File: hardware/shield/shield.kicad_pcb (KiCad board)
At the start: 2 copper layers, 83 parts, among them J1 Conn_01x18, J10 Conn_01x09, J11 Conn_01x03, J12 Conn_01x03, J13 Conn_01x04, J14 DCDC, J15 Conn_01x01_Pin, J16 Conn_01x01_Pin, J17 Conn_01x01_Pin, J18 Conn_01x01_Pin, J19 Conn_01x01_Pin, J2 Conn_01x20, J20 Conn_01x01_Pin, J21 Conn_01x01_Pin, J22 Conn_01x01_Pin, J23 Conn_01x01_Pin, J24 Conn_01x03, J25 Conn_01x03, J26 Conn_01x04, J27 Conn_01x03, J28 Conn_01x03, J29 Conn_01x03, J3 Conn_01x20, J30 Conn_01x03, J31 Conn_01x03, J32 Conn_01x08, J33 Conn_01x04, J34 DCDC, J35 Conn_01x03, J4 BAT, J5 DCDC, J6 DCDC, J7 Conn_01x03, J8 Conn_01x03, J9 Conn_01x10, U1 NUCLEO-N657X0-Q, U2 AMS1117-3.3

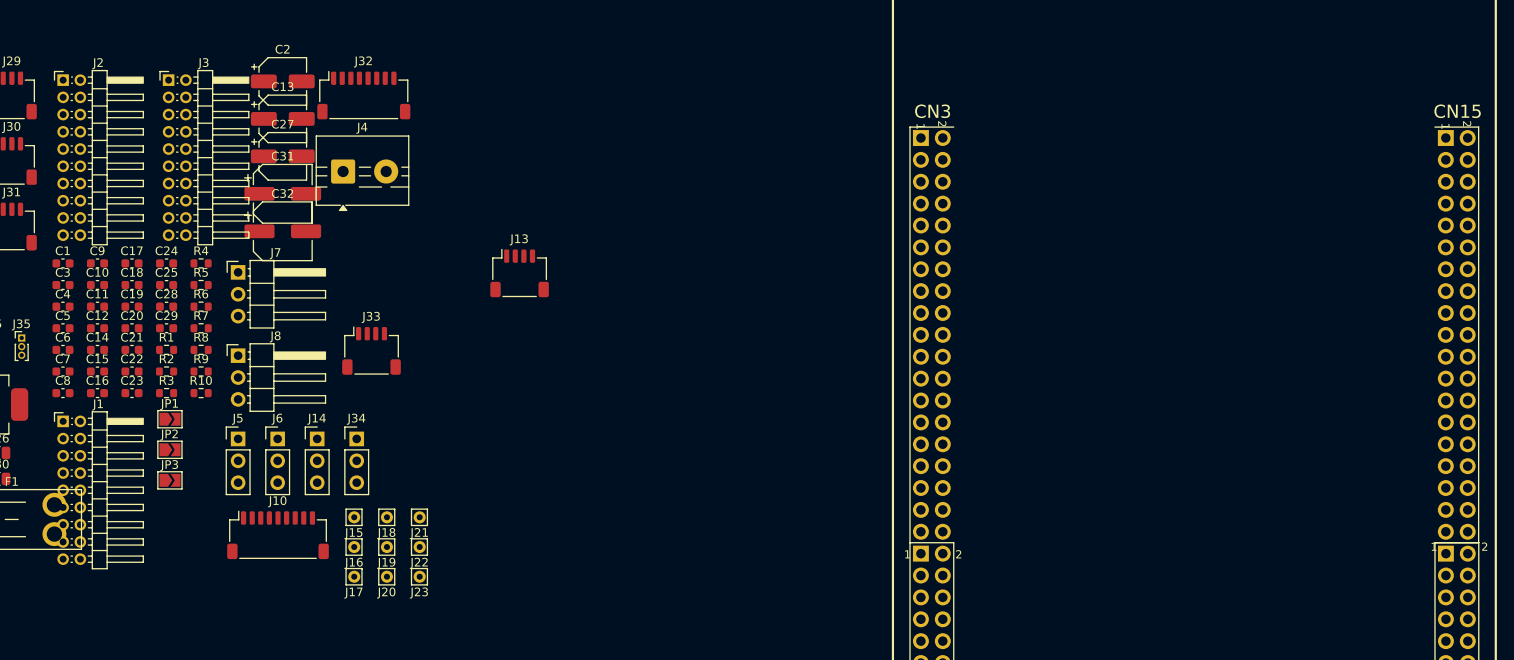
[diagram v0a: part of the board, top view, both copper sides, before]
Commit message: larger pin headers
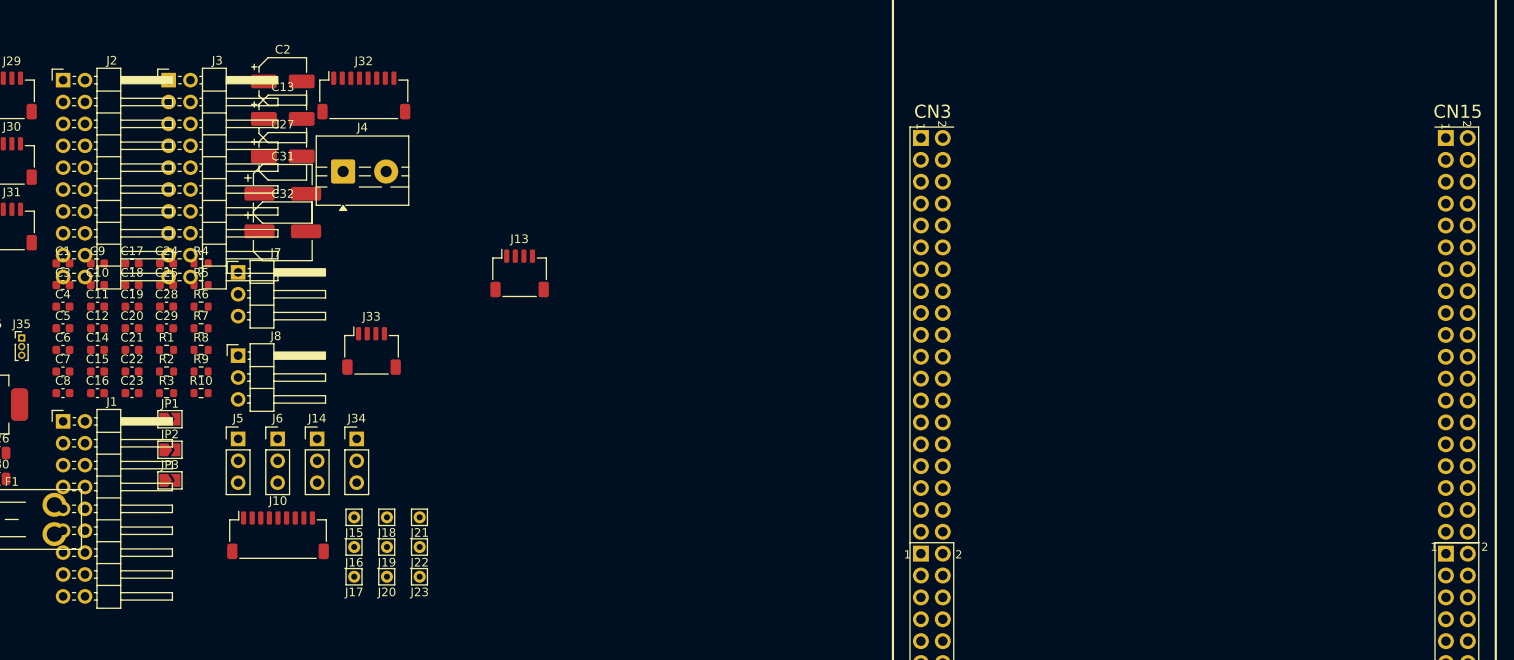
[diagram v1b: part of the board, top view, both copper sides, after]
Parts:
- J1: footprint Connector_PinHeader_2.00mm:PinHeader_2x09_P2.00mm_Horizontal -> Connector_PinHeader_2.54mm:PinHeader_2x09_P2.54mm_Horizontal
- J2, J3: footprint Connector_PinHeader_2.00mm:PinHeader_2x10_P2.00mm_Horizontal -> Connector_PinHeader_2.54mm:PinHeader_2x10_P2.54mm_Horizontal

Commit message: Approx layout done
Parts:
- J1: value Conn_01x18 -> CAMERA
- J10: value Conn_01x09 -> UI_MODULE
- J11: value Conn_01x03 -> RX_PWM
- J12: value Conn_01x03 -> CMD_RX
- J13: value Conn_01x04 -> TEL_UART
- J14: value DCDC -> 5V_DCDC_2
- J15: value Conn_01x01_Pin -> 5V_TP1
- J16: value Conn_01x01_Pin -> 5V_TP2
- J17: value Conn_01x01_Pin -> 3V3_TP3
- J18: value Conn_01x01_Pin -> 3V3_TP4
- J19: value Conn_01x01_Pin -> GND_TP1
- J2: value Conn_01x20 -> LINE_FRONT
- J20: value Conn_01x01_Pin -> GND_TP2
- J21: value Conn_01x01_Pin -> GND_TP3
- J22: value Conn_01x01_Pin -> GND_TP4
- J23: value Conn_01x01_Pin -> GND
- J24: value Conn_01x03 -> UART
- J25: value Conn_01x03 -> SPI
- J26: value Conn_01x04 -> PINS
- J27: value Conn_01x03 -> LED_DATA
- J28: value Conn_01x03 -> IR_1
- J29: value Conn_01x03 -> IR_2
- J3: value Conn_01x20 -> LINE_BACK
- J30: value Conn_01x03 -> IR_3
- J31: value Conn_01x03 -> IR_4
- J32: value Conn_01x08 -> MOTOR_DRIVER
- J33: value Conn_01x04 -> ENC_AB
- J34: value DCDC -> 8V_DCDC_2
- J35: value Conn_01x03 -> I2C4
- J5: value DCDC -> 5V_DCDC_1
- J6: value DCDC -> 8V_DCDC_1
- J7: value Conn_01x03 -> SERVO_BACK
- J8: value Conn_01x03 -> SERVO_FRONT
- J9: value Conn_01x10 -> IMU
- JP1: value SolderJumper_2_Open -> 5V_1
- JP2: value SolderJumper_2_Open -> 5V_2
- JP3: value SolderJumper_2_Open -> 3V3
- moved J1 175.6 mm to (232.5, 45.0)
- moved J2 174.2 mm to (232.5, 78.6)
- moved C6 169.9 mm to (221.5, 133.6), turned to 90 degrees
- moved J8 162.6 mm to (235.0, 131.7)
- moved U1 159.3 mm to (35.4, 51.8), turned to -90 degrees
- moved R2 157.4 mm to (228.0, 49.5), turned to 90 degrees
- moved C32 155.9 mm to (227.5, 130.3), turned to 90 degrees
- moved R1 155.0 mm to (225.5, 46.8), turned to 90 degrees
- moved F1 146.4 mm to (186.9, 41.4), turned to 180 degrees
- moved J30 136.3 mm to (191.6, 62.2), turned to 90 degrees
- moved J31 136.0 mm to (191.1, 72.7), turned to 90 degrees
- moved J28 131.6 mm to (179.0, 62.3), turned to 90 degrees
- moved J29 126.1 mm to (179.0, 72.8), turned to 90 degrees
- moved C5 123.5 mm to (182.0, 47.3), turned to -90 degrees
- moved C21 121.7 mm to (189.5, 56.9), turned to 90 degrees
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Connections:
- J27 pad 2: Net-(J27-Pin_2) -> 5V_EXT
- J27 pad 3: 5V_EXT -> Net-(J27-Pin_3)
- R5 pad 1: Net-(J27-Pin_2) -> Net-(J27-Pin_3)
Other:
- board outline added: 230 x 110 mm

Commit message: PCB v1 done
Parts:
- moved J25 186.9 mm to (202.0, 87.5), turned to 0 degrees
- moved C14 129.2 mm to (216.2, 111.4)
- moved J13 129.2 mm to (218.7, 116.9)
- moved C4 128.8 mm to (224.5, 137.7)
- moved C1 128.6 mm to (33.0, 35.5), turned to 90 degrees
- moved J34 128.5 mm to (37.0, 35.0)
- moved C13 127.3 mm to (201.5, 131.1), turned to 180 degrees
- moved JP2 126.8 mm to (201.5, 136.9)
- moved C12 126.2 mm to (196.4, 133.7)
- moved J14 123.8 mm to (210.0, 124.9)
- moved J6 122.2 mm to (219.5, 133.2)
- moved C27 120.4 mm to (174.0, 73.0)
- moved JP3 120.4 mm to (192.5, 78.8)
- moved U2 120.4 mm to (184.7, 74.3)
- moved C26 120.4 mm to (192.9, 74.3)
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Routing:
- net 3V3: track 0.00 -> 492.8 mm, vias 0 -> 13
- net VBAT: track 0.00 -> 471.4 mm, vias 0 -> 1
- net 5V: track 0.00 -> 334.4 mm, vias 0 -> 8
- net /LINE_AD_CS2: track 0.00 -> 304.3 mm, vias 0 -> 3
- net /LINE_AD_CS1: track 0.00 -> 301.7 mm, vias 0 -> 8
- net /LINE_LED_OE: track 0.00 -> 273.0 mm, vias 0 -> 4
- net /TEL_TX: track 0.00 -> 253.3 mm, vias 0 -> 6
- net /LINE_SPI4_SCK: track 0.00 -> 251.4 mm, vias 0 -> 2
- net /OV_I2C4_SCL: track 0.00 -> 250.4 mm, vias 0 -> 13
- net /LINE_AD_CS3: track 0.00 -> 248.6 mm, vias 0 -> 7
- net /LINE_INF_OE: track 0.00 -> 240.9 mm, vias 0 -> 7
- net /LINE_INF_LE: track 0.00 -> 238.1 mm, vias 0 -> 7
- net /LINE_LED_LE: track 0.00 -> 235.1 mm, vias 0 -> 7
- net /SERVO_FRONT: track 0.00 -> 234.0 mm, vias 0 -> 11
- net /LINE_SPI4_MOSI: track 0.00 -> 234.0 mm, vias 0 -> 1
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- added copper zone on B.Cu, net GND
- added copper zone on F.Cu, net GND

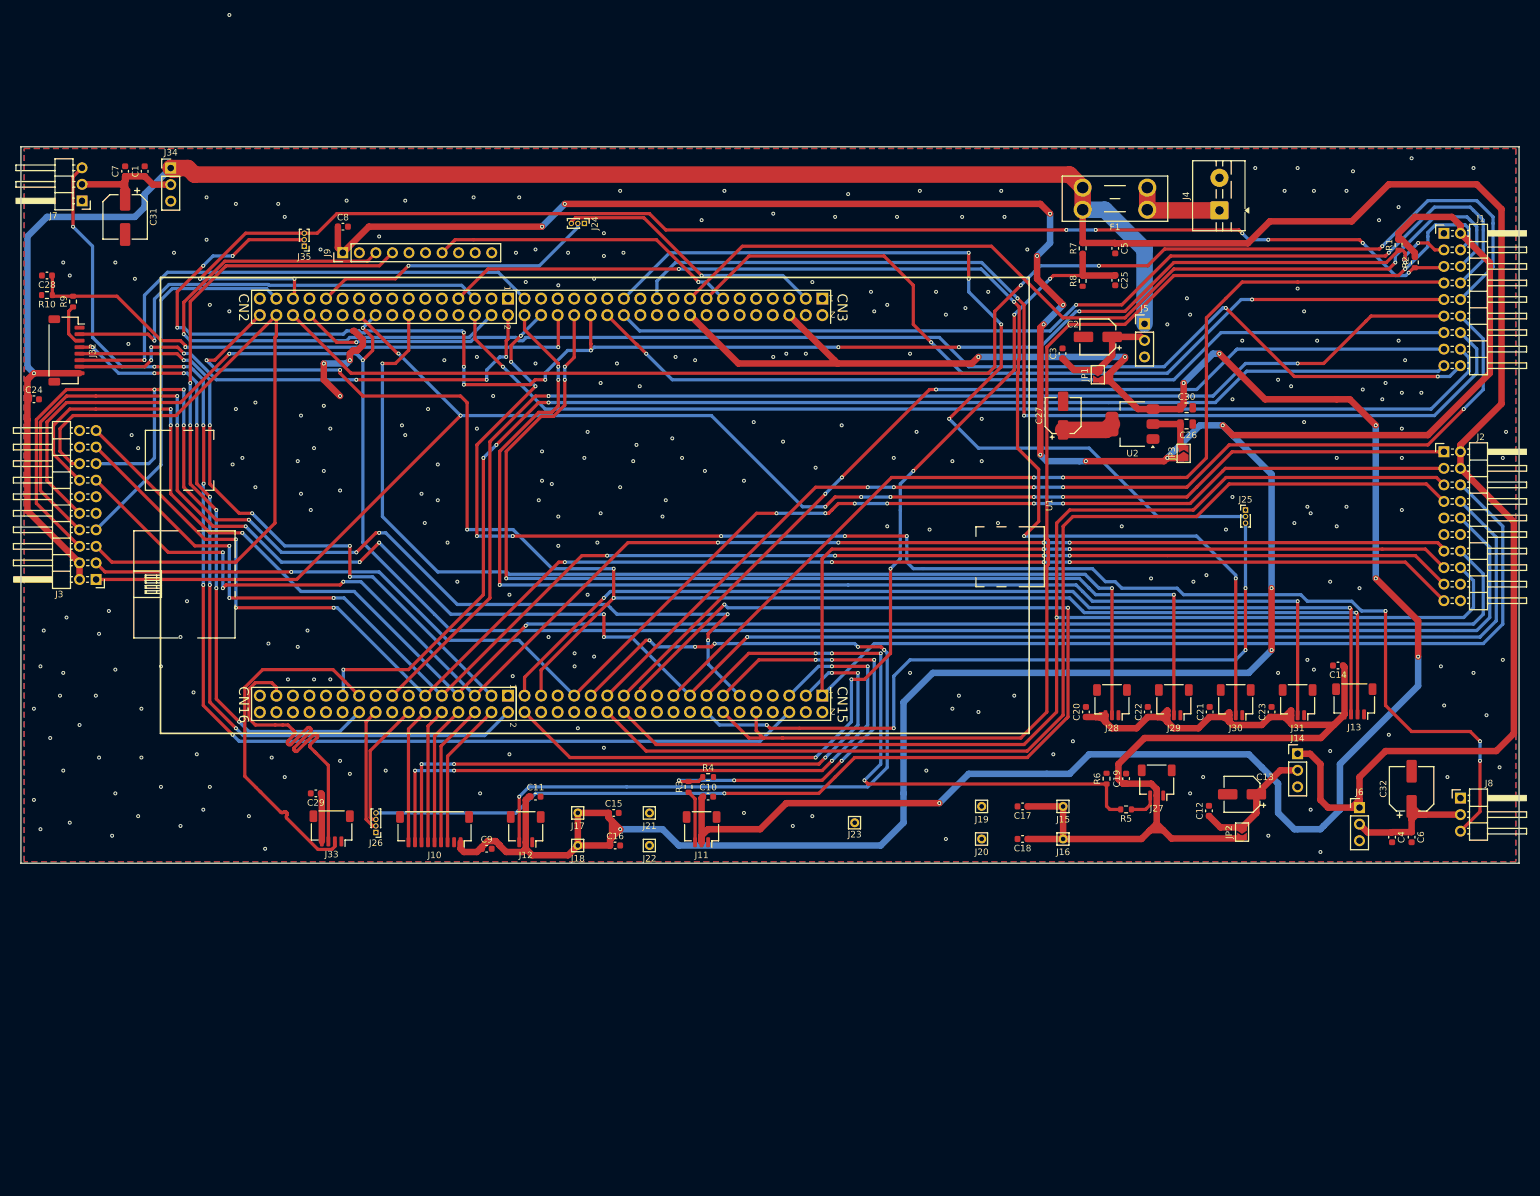
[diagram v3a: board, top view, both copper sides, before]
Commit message: Fixed DRCs, added labels to silkscreen
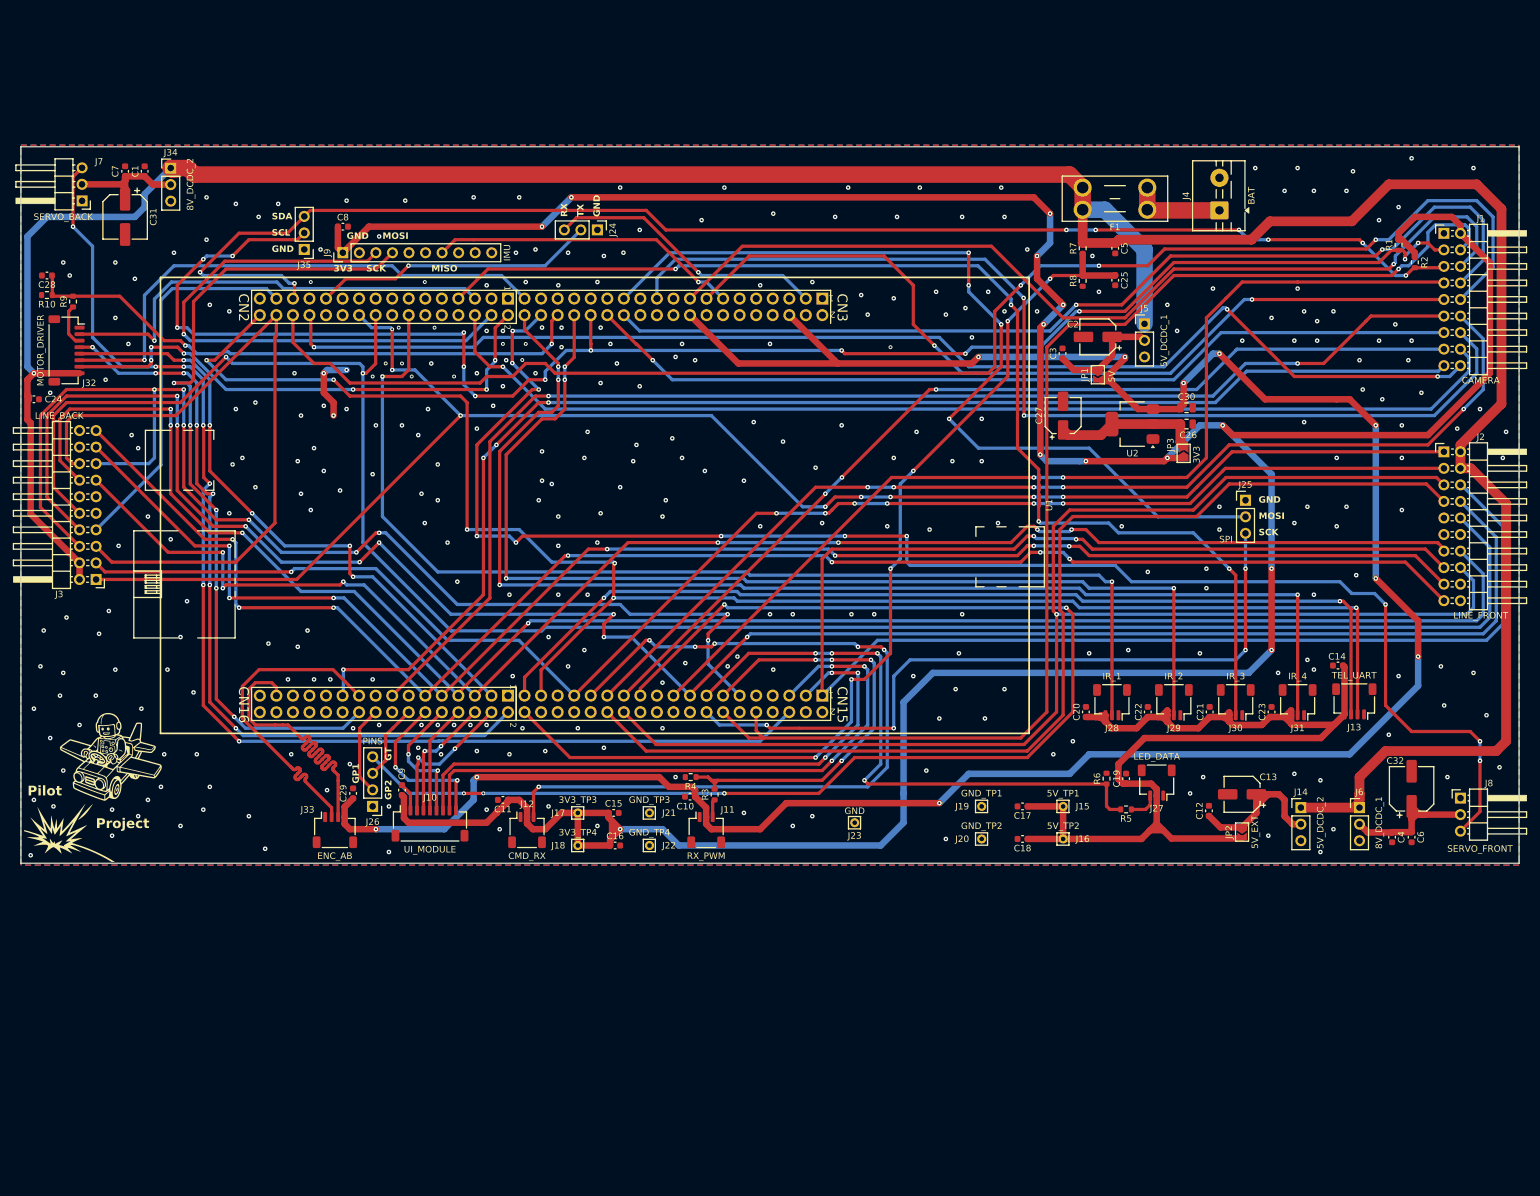
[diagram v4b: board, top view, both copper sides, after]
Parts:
- added G***: LOGO, LOGO, F.Cu at (29.5, 130.0)
- J24, J25, J35: footprint Connector_PinHeader_1.00mm:PinHeader_1x03_P1.00mm_Vertical -> Connector_PinHeader_2.54mm:PinHeader_1x03_P2.54mm_Vertical
- J26: footprint Connector_PinHeader_1.00mm:PinHeader_1x04_P1.00mm_Vertical -> Connector_PinHeader_2.54mm:PinHeader_1x04_P2.54mm_Vertical
- JP1: value 5V_1 -> 5V
- JP2: value 5V_2 -> 5V_EXT
- moved C9 15.8 mm to (72.5, 130.5), turned to 90 degrees
- moved J14 8.28 mm to (210.5, 133.2)
- moved C29 5.73 mm to (65.0, 131.0), turned to 90 degrees
- moved C11 5.02 mm to (88.0, 132.0), turned to 180 degrees
- moved R3 4.17 mm to (120.5, 131.2)
- moved J26 4.03 mm to (68.0, 133.0)
- moved C10 2.78 mm to (116.7, 131.5), turned to 180 degrees
- moved R4 2.67 mm to (116.8, 128.5), turned to 180 degrees
- moved J24 2.24 mm to (102.5, 44.5)
- moved J25 1.50 mm to (202.0, 86.0)
- moved J10 1.12 mm to (76.8, 135.6), turned to 0 degrees
- moved J11 0.71 mm to (119.2, 136.6), turned to 0 degrees
- moved J33 0.56 mm to (62.2, 136.6), turned to 0 degrees
- moved J35 0.50 mm to (57.5, 47.5)
- moved J12 0.24 mm to (91.7, 136.6), turned to 0 degrees
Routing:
- net 5V: track 334.4 -> 374.7 mm, vias 8 -> 10
- net /UI_SDA: track 106.3 -> 95.4 mm, vias 5 -> 3
- net /UI_SCL: track 98.9 -> 89.8 mm, vias 5 -> 3
- net /GEN_PIN1: track 19.6 -> 11.7 mm
- net Net-(JP3-B): track 15.9 -> 23.1 mm
- net 3V3: track 492.8 -> 499.7 mm
- net /CMD_RX: track 133.2 -> 127.5 mm
- net /GEN_PIN2: track 19.0 -> 13.8 mm
- net Net-(J14-Pin_2): track 19.7 -> 24.6 mm
- net /OV_D1: track 219.7 -> 224.6 mm
- net Net-(J11-Pin_3): track 8.09 -> 3.25 mm
- net /UI_B: track 21.5 -> 16.9 mm
- net /UI_CONF: track 21.0 -> 25.4 mm, vias 0 -> 2
- net /ENC_A: track 54.1 -> 49.9 mm
- net /IR_3: track 184.4 -> 180.3 mm
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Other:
- board text added: "3V3"
- board text added: "GND"
- board text added: "GP1"
- board text added: "GP2"
- board text added: "GT"
- board text added: "MISO"
- board text added: "MOSI"
- board text added: "Pilot"
- board text added: "Project"
- board text added: "RX"
- board text added: "SCK"
- board text added: "SCL"
- board text added: "SDA"
- board text added: "TX"
